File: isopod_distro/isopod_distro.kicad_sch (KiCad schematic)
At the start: 35 parts

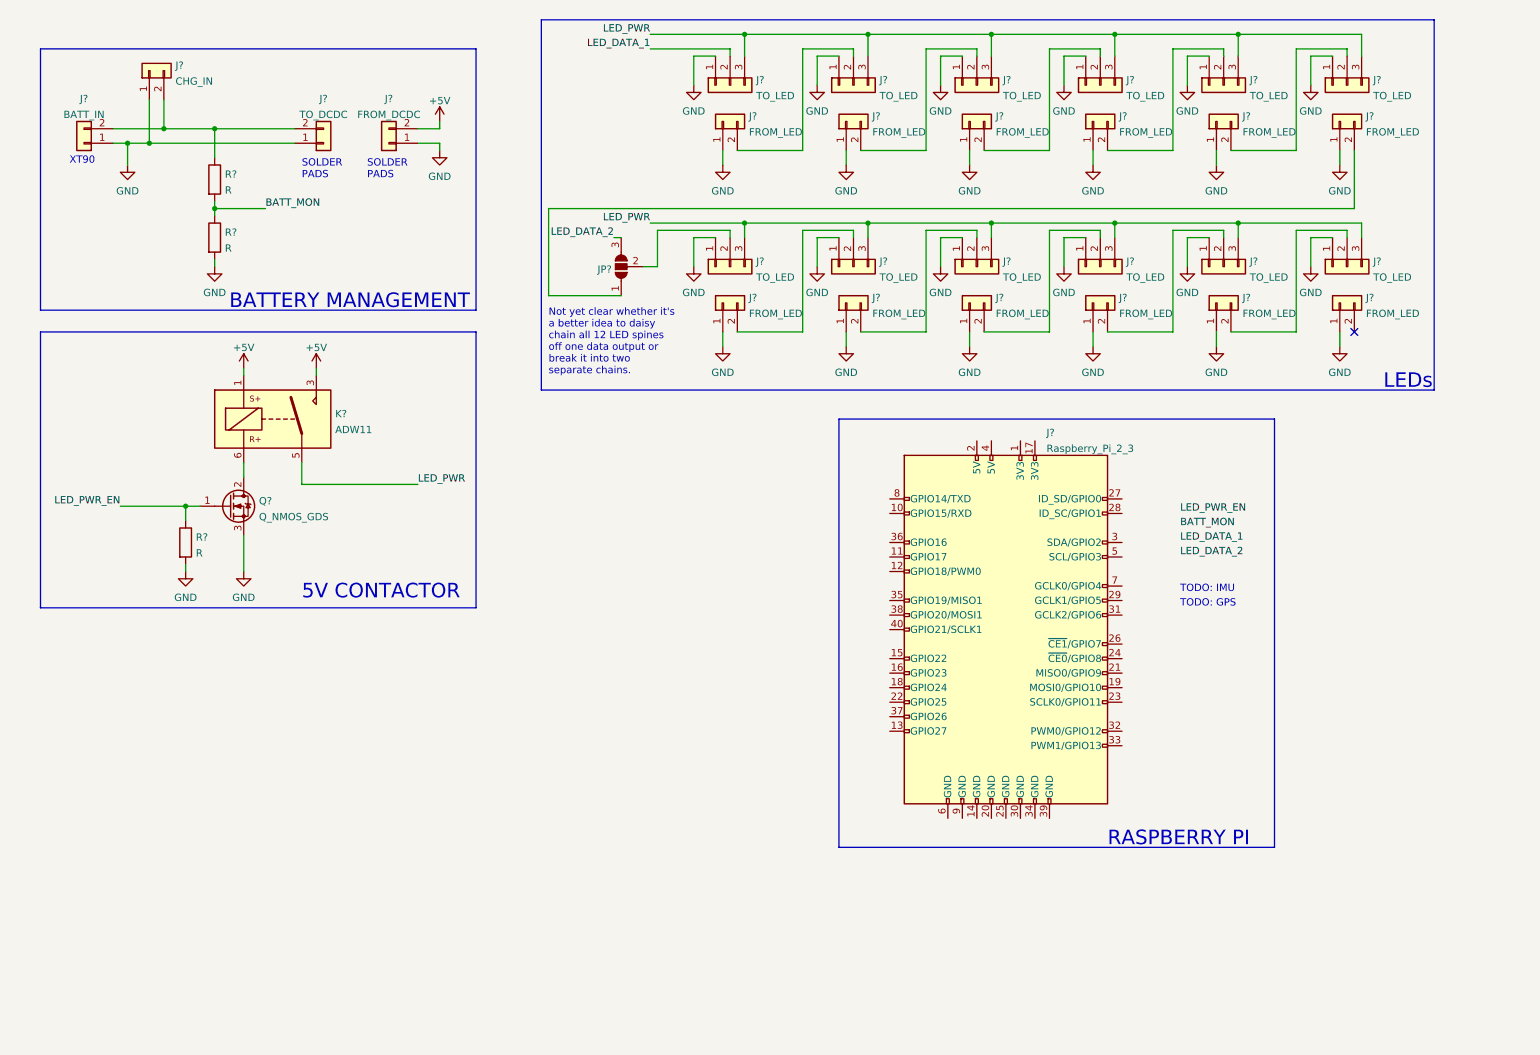
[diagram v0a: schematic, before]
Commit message: First draft of schematic and pcb placement
Finish first draft of schematic:
* Replace relay with hexFET switch
* Replace battery monitoring tap with fuel gauge / balance IC
* Fill in various values
* Pi pin assigments
* Footprint assignments
    * Except for the power resistors around the fuel gauge

PCB:
* Draw Pi HAT PCB outline and place expansion header
* Rough placement of most components
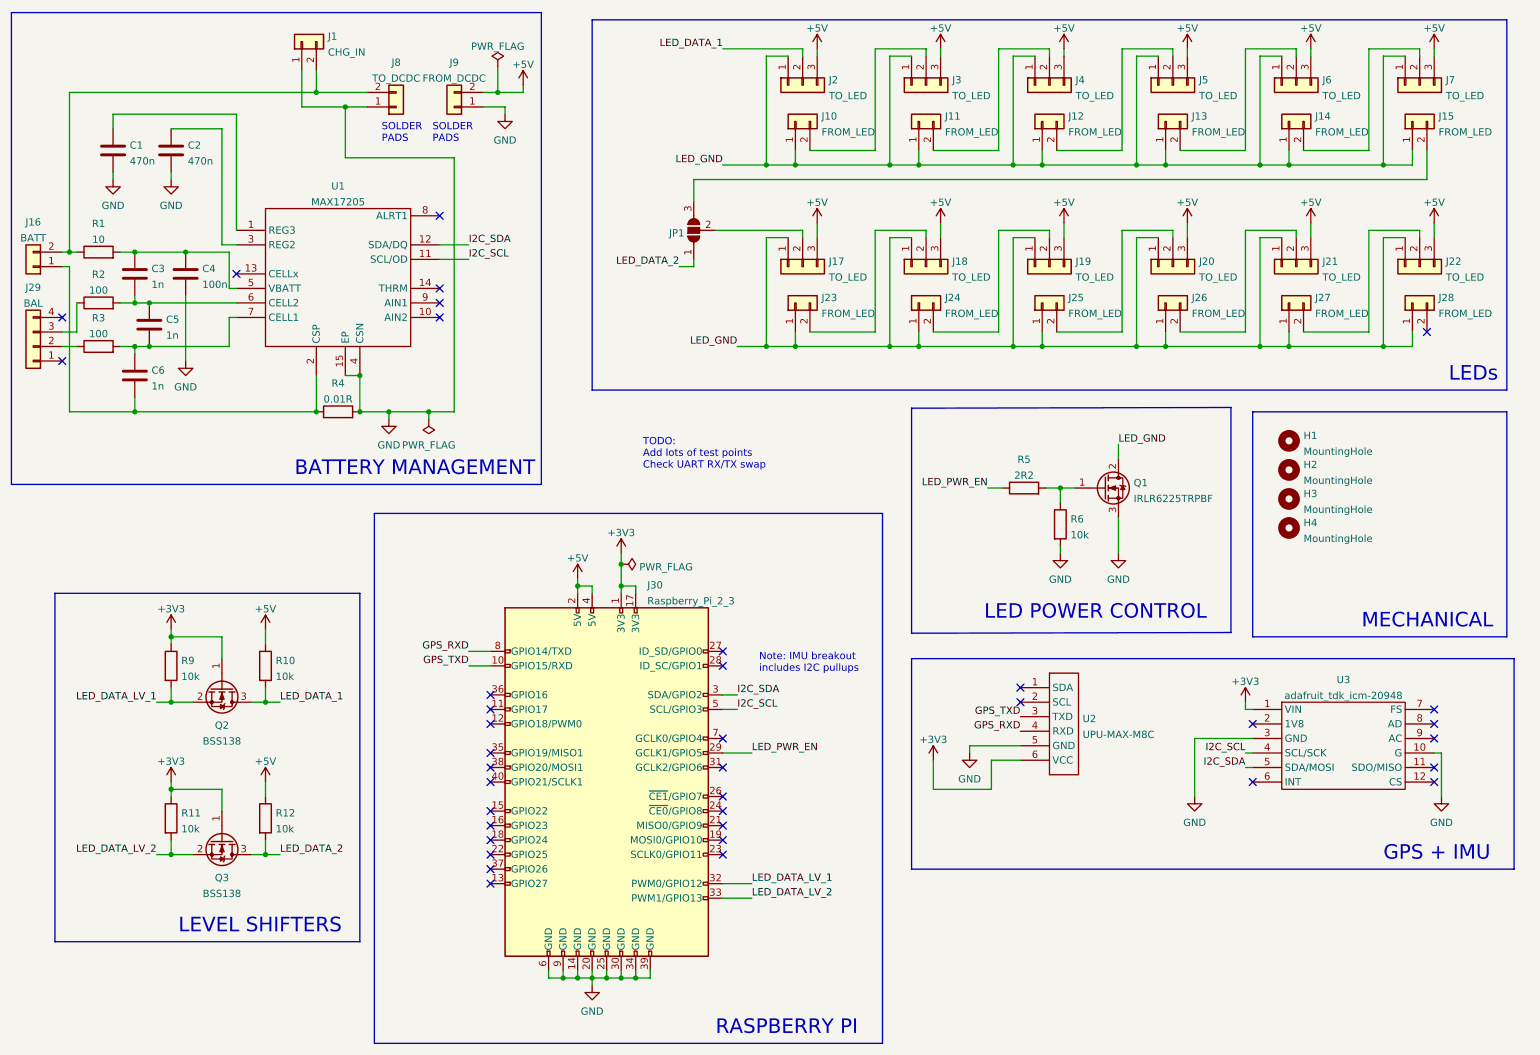
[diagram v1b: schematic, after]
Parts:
- removed K?: ADW11, Relay_THT:Relay_1P1T_NO_10x24x18.8mm_Panasonic_ADW11xxxxW_THT, symbol Relay:ADW11
- removed R? (x2): R, symbol Device:R
- added C1, C2: 470n, Capacitor_SMD:C_0603_1608Metric_Pad1.08x0.95mm_HandSolder, symbol Device:C
- added C3, C5, C6: 1n, Capacitor_SMD:C_0603_1608Metric_Pad1.08x0.95mm_HandSolder, symbol Device:C
- added C4: 100n, Capacitor_SMD:C_0603_1608Metric_Pad1.08x0.95mm_HandSolder, symbol Device:C
- added H1, H2, H3, H4: MountingHole, MountingHole:MountingHole_2.7mm, symbol Mechanical:MountingHole
- added J29: BAL, Connector_JST:JST_XH_B4B-XH-AM_1x04_P2.50mm_Vertical, symbol Connector_Generic:Conn_01x04
- added Q2, Q3: BSS138, Package_TO_SOT_SMD:SOT-23, symbol Transistor_FET:BSS138
- added R1: 10, symbol Device:R
- added R10, R11, R12, R9: 10k, Resistor_SMD:R_0603_1608Metric_Pad0.98x0.95mm_HandSolder, symbol Device:R
- added R2, R3: 100, symbol Device:R
- added R4: 0.01R, symbol Device:R
- added R5: 2R2, Resistor_SMD:R_0603_1608Metric_Pad0.98x0.95mm_HandSolder, symbol Device:R
- added U1: MAX17205, Package_DFN_QFN:TDFN-14-1EP_3x3mm_P0.4mm_EP1.78x2.35mm, symbol MAX17205:MAX17205
- added U2: UPU-MAX-M8C, upu-max-m8c:upu-max-m8c, symbol UPU-MAX-M8C:UPU-MAX-M8C
- added U3: adafruit_tdk_icm-20948, adafruit-tdk-icm-20948:adafruit-tdk-icm-20948, symbol adafruit_tdk_icm-20948:adafruit_tdk_icm-20948
- J1, J8, J9: renamed from J?; footprint (none) -> TestPoint:TestPoint_2Pads_Pitch5.08mm_Drill1.3mm
- J10, J11, J12, J13, J14, J15, J23, J24, J25, J26, J27, J28: renamed from J?; footprint (none) -> Connector_Molex:Molex_KK-254_AE-6410-02A_1x02_P2.54mm_Vertical
- J16: renamed from J?; value BATT_IN -> BATT; footprint (none) -> Connector_AMASS:AMASS_XT60-M_1x02_P7.20mm_Vertical
- J17, J18, J19, J2, J20, J21, J22, J3, J4, J5, J6, J7: renamed from J?; footprint (none) -> Connector_Molex:Molex_KK-254_AE-6410-03A_1x03_P2.54mm_Vertical
- J30: renamed from J?; footprint (none) -> Connector_PinHeader_2.54mm:PinHeader_2x20_P2.54mm_Vertical
- JP1: renamed from JP?; footprint (none) -> Jumper:SolderJumper-3_P1.3mm_Bridged12_RoundedPad1.0x1.5mm
- Q1: renamed from Q?; value Q_NMOS_GDS -> IRLR6225TRPBF; footprint (none) -> Package_TO_SOT_SMD:TO-252-2
- R6: renamed from R?; value R -> 10k; footprint (none) -> Resistor_SMD:R_0603_1608Metric_Pad0.98x0.95mm_HandSolder
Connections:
- net LED_PWR is gone; now on net +5V: J17.3 (Pin_3), J18.3 (Pin_3), J19.3 (Pin_3), J2.3 (Pin_3), J20.3 (Pin_3), J21.3 (Pin_3), J22.3 (Pin_3), J3.3 (Pin_3), J4.3 (Pin_3), J5.3 (Pin_3), J6.3 (Pin_3), J7.3 (Pin_3)
- net +5V: now also J30.2 (5V), J30.4 (5V), R10.1, R12.1
- net GND: now also J30.14 (GND), J30.20 (GND), J30.25 (GND), J30.30 (GND), J30.34 (GND), J30.39 (GND), J30.6 (GND), J30.9 (GND), C1.2, C2.2, C4.2, R4.2, U1.15 (EP), U1.4 (CSN), U2.5 (GND), U3.10 (G), U3.3 (GND); no longer J10.1 (Pin_1), J11.1 (Pin_1), J12.1 (Pin_1), J13.1 (Pin_1), J14.1 (Pin_1), J15.1 (Pin_1), J16.1 (Pin_1), J17.1 (Pin_1), J18.1 (Pin_1), J19.1 (Pin_1), J2.1 (Pin_1), J20.1 (Pin_1), J21.1 (Pin_1), J22.1 (Pin_1), J23.1 (Pin_1), J24.1 (Pin_1), J25.1 (Pin_1), J26.1 (Pin_1), J27.1 (Pin_1), J28.1 (Pin_1), J3.1 (Pin_1), J4.1 (Pin_1), J5.1 (Pin_1), J6.1 (Pin_1), J7.1 (Pin_1)
- net LED_DATA_1: now also Q2.3 (D), R10.2
- net LED_DATA_2: now also JP1.1 (A), Q3.3 (D), R12.2; no longer JP1.3 (B)
- net LED_PWR_EN: now also J30.29 (GCLK1/GPIO5), R5.1; no longer Q1.1 (G), R6.1
- net +3V3: now reaches J30.1 (3V3)
- net +3V3: now also J30.17 (3V3), Q2.1 (G), Q3.1 (G), R11.1, R9.1, U2.6 (VCC), U3.1 (VIN)
- net GPS_TXD: now reaches J30.10 (GPIO15/RXD)
- net GPS_TXD: now also U2.3 (TXD)
- net I2C_SDA: now reaches J30.3 (SDA/GPIO2)
- net I2C_SDA: now also U1.12 (SDA/DQ), U3.5 (SDA/MOSI)
- net LED_DATA_LV_1: now reaches J30.32 (PWM0/GPIO12)
- net LED_DATA_LV_1: now also Q2.2 (S), R9.2
- net LED_DATA_LV_2: now reaches J30.33 (PWM1/GPIO13)
- net LED_DATA_LV_2: now also Q3.2 (S), R11.2
- net I2C_SCL: now reaches J30.5 (SCL/GPIO3)
- net I2C_SCL: now also U1.11 (SCL/OD), U3.4 (SCL/SCK)
- net GPS_RXD: now reaches J30.8 (GPIO14/TXD)
- net GPS_RXD: now also U2.4 (RXD)
- net at J1.2 (Pin_2), J16.2 (Pin_2), J8.2 (Pin_2): now also R1.1
- net at J15.2 (Pin_2): now also JP1.3 (B); no longer JP1.1 (A)
- net LED_GND: now reaches Q1.2 (D)
- net LED_GND: now also J10.1 (Pin_1), J11.1 (Pin_1), J12.1 (Pin_1), J13.1 (Pin_1), J14.1 (Pin_1), J15.1 (Pin_1), J17.1 (Pin_1), J18.1 (Pin_1), J19.1 (Pin_1), J2.1 (Pin_1), J20.1 (Pin_1), J21.1 (Pin_1), J22.1 (Pin_1), J23.1 (Pin_1), J24.1 (Pin_1), J25.1 (Pin_1), J26.1 (Pin_1), J27.1 (Pin_1), J28.1 (Pin_1), J3.1 (Pin_1), J4.1 (Pin_1), J5.1 (Pin_1), J6.1 (Pin_1), J7.1 (Pin_1)
- new net: C3.1, C4.1, R1.2, U1.5 (VBATT)
- new net: Q1.1 (G), R5.2, R6.1
- new net: J29.3 (Pin_3), R2.1
- new net: C3.2, C5.1, R2.2, U1.6 (CELL2)
- new net: C1.1, U1.1 (REG3)
- new net: C5.2, C6.1, R3.2, U1.7 (CELL1)
- new net: C6.2, J16.1 (Pin_1), R4.1, U1.2 (CSP)
- new net: C2.1, U1.3 (REG2)
- new net: J29.2 (Pin_2), R3.1
- no-connect marks 1 -> 38
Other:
- note added: "GPS + IMU"
- note added: "LED POWER CONTROL"
- note added: "LEVEL SHIFTERS"
- note added: "MECHANICAL"
- note added: "Note: IMU breakout includes I2C pullups"
- note added: "TODO: Add lots of test points Check UART RX/TX swap"
- note removed: "5V CONTACTOR"
- note removed: "Not yet clear whether it's a better idea to daisy chain all 12 LED spines off one data output or break it into two separate chains."
- note removed: "TODO: GPS"
- note removed: "TODO: IMU"
- note removed: "XT90"
- company: (none) -> David Turner
- title: (none) -> Isopod distro
- moved on the sheet: J1, J10, J11, J12, J13, J14, J15, J16, J17, J18, J19, J2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

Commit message: Assign footprints for fuel gauge resistors
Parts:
- R1, R2, R3: footprint (none) -> Resistor_SMD:R_0805_2012Metric_Pad1.20x1.40mm_HandSolder
- R4: footprint (none) -> Resistor_SMD:R_1206_3216Metric_Pad1.30x1.75mm_HandSolder
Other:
- note removed: "TODO: Add lots of test points Check UART RX/TX swap"
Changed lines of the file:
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@@
-    (effects (font (size 1.27 1.27)) (justify left bottom))
-  )
-  (text "TODO:\nAdd lots of test points\nCheck UART RX/TX swap"
-    (at 130.81 93.98 0)
     (effects (font (size 1.27 1.27)) (justify left bottom))
   )
@@
     (property "Reference" "R1" (id 0) (at 35.56 50.8975 90))
     (property "Value" "10" (id 1) (at 35.56 53.6726 90))
-    (property "Footprint" "" (id 2) (at 35.56 57.658 90)
+    (property "Footprint" "Resistor_SMD:R_0805_2012Metric_Pad1.20x1.40mm_HandSolder" (id 2) (at 35.56 57.658 90)
       (effects (font (size 1.27 1.27)) hide)
     )
@@
     (property "Reference" "R2" (id 0) (at 35.56 59.7875 90))
     (property "Value" "100" (id 1) (at 35.56 62.5626 90))
-    (property "Footprint" "" (id 2) (at 35.56 66.548 90)
+    (property "Footprint" "Resistor_SMD:R_0805_2012Metric_Pad1.20x1.40mm_HandSolder" (id 2) (at 35.56 66.548 90)
       (effects (font (size 1.27 1.27)) hide)
     )
@@
     (property "Reference" "R4" (id 0) (at 77.47 78.8375 90))
     (property "Value" "0.01R" (id 1) (at 77.47 81.6126 90))
-    (property "Footprint" "" (id 2) (at 77.47 85.598 90)
+    (property "Footprint" "Resistor_SMD:R_1206_3216Metric_Pad1.30x1.75mm_HandSolder" (id 2) (at 77.47 85.598 90)
       (effects (font (size 1.27 1.27)) hide)
     )
@@
     (property "Reference" "R3" (id 0) (at 35.56 67.4075 90))
     (property "Value" "100" (id 1) (at 35.56 70.1826 90))
-    (property "Footprint" "" (id 2) (at 35.56 74.168 90)
+    (property "Footprint" "Resistor_SMD:R_0805_2012Metric_Pad1.20x1.40mm_HandSolder" (id 2) (at 35.56 74.168 90)
       (effects (font (size 1.27 1.27)) hide)
     )
@@
     )
     (path "/03e2a6c0-3483-4c66-80ca-6eb6645cf8e5"
-      (reference "R1") (unit 1) (value "10") (footprint "")
+      (reference "R1") (unit 1) (value "10") (footprint "Resistor_SMD:R_0805_2012Metric_Pad1.20x1.40mm_HandSolder")
     )
     (path "/1bf446fd-88c1-4de3-9409-62fdf282a99f"
-      (reference "R2") (unit 1) (value "100") (footprint "")
+      (reference "R2") (unit 1) (value "100") (footprint "Resistor_SMD:R_0805_2012Metric_Pad1.20x1.40mm_HandSolder")
     )
     (path "/bc121d9f-4d13-43b5-94f9-b392300085f2"
-      (reference "R3") (unit 1) (value "100") (footprint "")
+      (reference "R3") (unit 1) (value "100") (footprint "Resistor_SMD:R_0805_2012Metric_Pad1.20x1.40mm_HandSolder")
     )
     (path "/6bbf2dd3-15a1-483b-8eec-e005bb8e7217"
-      (reference "R4") (unit 1) (value "0.01R") (footprint "")
+      (reference "R4") (unit 1) (value "0.01R") (footprint "Resistor_SMD:R_1206_3216Metric_Pad1.30x1.75mm_HandSolder")
     )
     (path "/715d37ea-5a71-47b3-80f7-1a42a8b131cc"

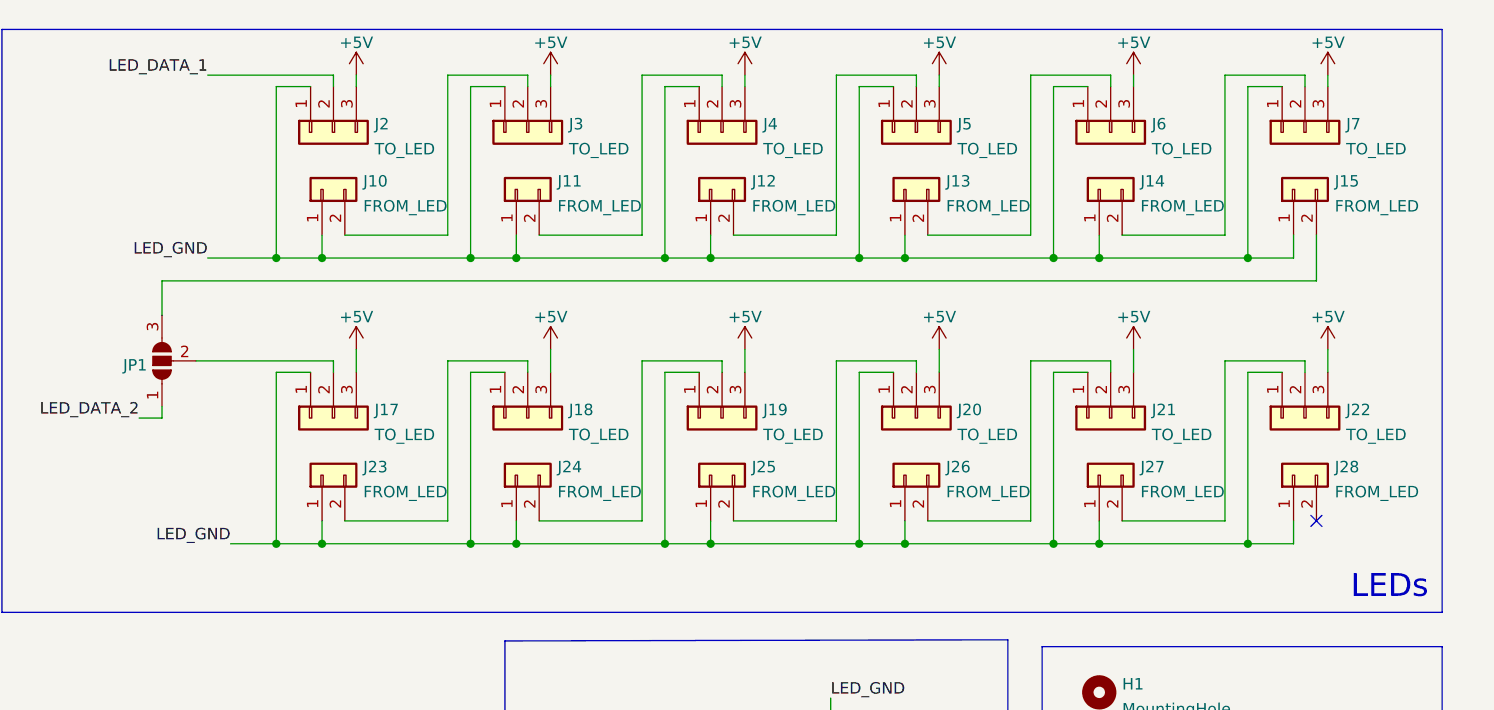
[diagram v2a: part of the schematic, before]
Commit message: 3-pin connectors for LED return, reroute
* Use 3-pin connectors for LED return so we can supply power at both
  ends of the LED strip
* Juggle placement of the PCB again
* First draft of PCB routing
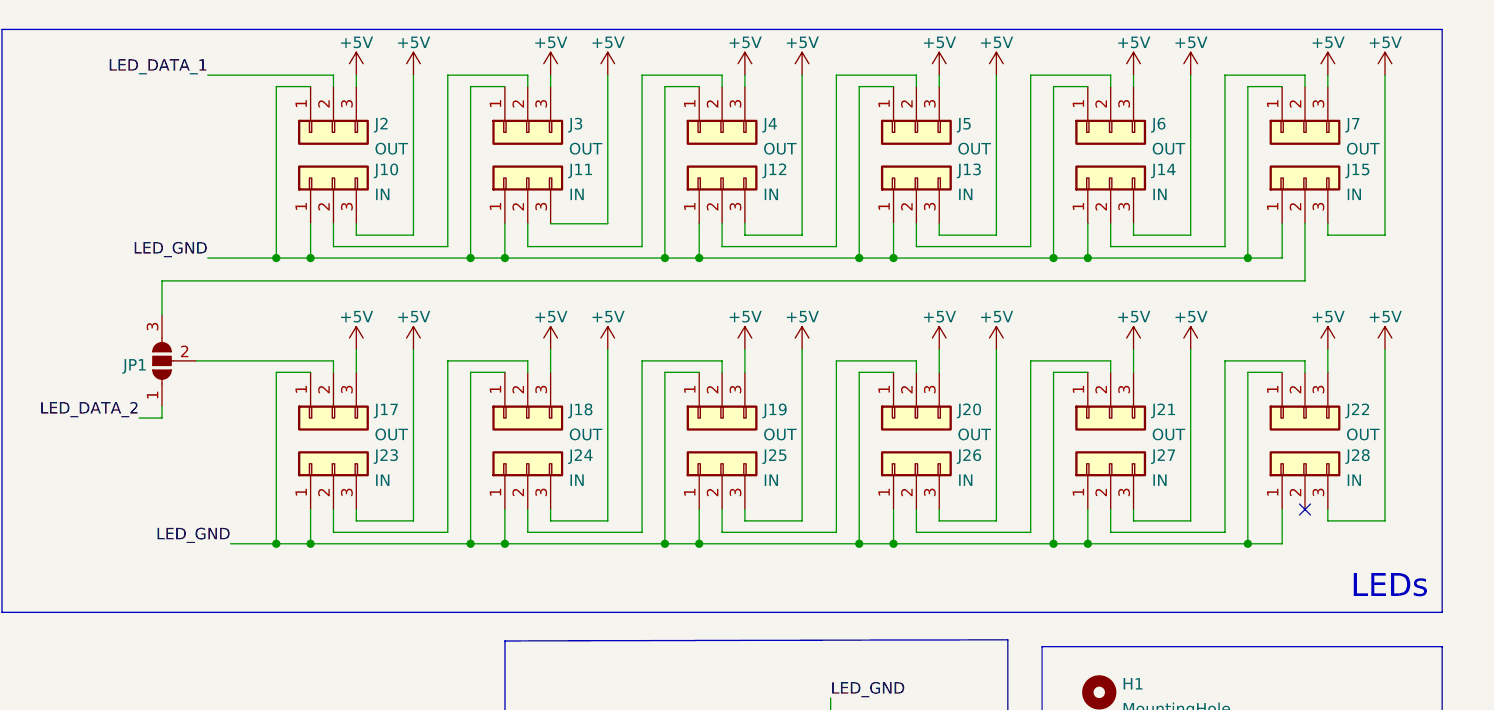
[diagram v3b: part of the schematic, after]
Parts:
- removed J10, J11, J12, J13, J14, J15, J23, J24, J25, J26, J27, J28: FROM_LED, Connector_Molex:Molex_KK-254_AE-6410-02A_1x02_P2.54mm_Vertical, symbol Connector_Generic:Conn_01x02
- added J10, J11, J12, J13, J14, J15, J23, J24, J25, J26, J27, J28: IN, Connector_Molex:Molex_KK-254_AE-6410-03A_1x03_P2.54mm_Vertical, symbol Connector_Generic:Conn_01x03
- J17, J18, J19, J2, J20, J21, J22, J3, J4, J5, J6, J7: value TO_LED -> OUT
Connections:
- net +5V: now also J10.3 (Pin_3), J11.3 (Pin_3), J12.3 (Pin_3), J13.3 (Pin_3), J14.3 (Pin_3), J15.3 (Pin_3), J23.3 (Pin_3), J24.3 (Pin_3), J25.3 (Pin_3), J26.3 (Pin_3), J27.3 (Pin_3), J28.3 (Pin_3)
- net LED_GND: now also J10.1 (Pin_1), J11.1 (Pin_1), J12.1 (Pin_1), J13.1 (Pin_1), J14.1 (Pin_1), J15.1 (Pin_1), J23.1 (Pin_1), J24.1 (Pin_1), J25.1 (Pin_1), J26.1 (Pin_1), J27.1 (Pin_1), J28.1 (Pin_1)
- net at J3.2 (Pin_2): now also J10.2 (Pin_2)
- net at J5.2 (Pin_2): now also J12.2 (Pin_2)
- net at J20.2 (Pin_2): now also J25.2 (Pin_2)
- net at J7.2 (Pin_2): now also J14.2 (Pin_2)
- net at J6.2 (Pin_2): now also J13.2 (Pin_2)
- net at JP1.3 (B): now also J15.2 (Pin_2)
- net at J19.2 (Pin_2): now also J24.2 (Pin_2)
- net at J22.2 (Pin_2): now also J27.2 (Pin_2)
- net at J21.2 (Pin_2): now also J26.2 (Pin_2)
- net at J18.2 (Pin_2): now also J23.2 (Pin_2)
- net at J4.2 (Pin_2): now also J11.2 (Pin_2)
